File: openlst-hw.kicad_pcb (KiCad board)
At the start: 4 copper layers, 85 x 85 mm, 123 parts, among them J1 Conn_02x20_Odd_Even, J10 EXT VBUS, J2 EXT 3.3V, J3 UART0, J4 UART1, J5 Switch Select, J6 Control Outputs, J7 CC Prog/Debug, J8 Conn_Coaxial, J9 ANT, U1 ADP150AUJZ-3.3-R7, U2 CC1110, U3 0433BM15A0001, U4 MIC803, U5 PE4250MLI, U6 PE4250MLI, U7 SF2446E, U8 RFFM6406, X1 TG2520SMN 27MHz

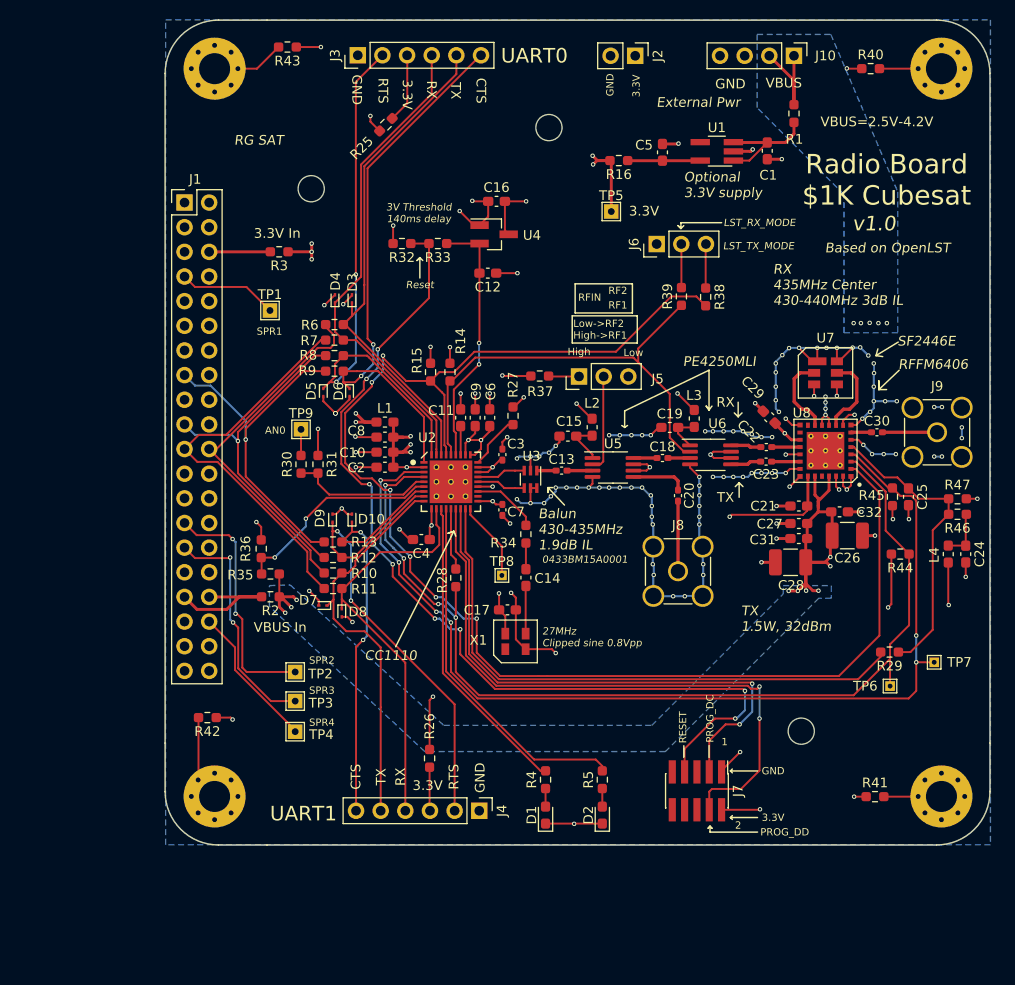
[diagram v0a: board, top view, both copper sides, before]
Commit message: upgrade to KICAD 8, change power converters and auxiliarry pin connectors
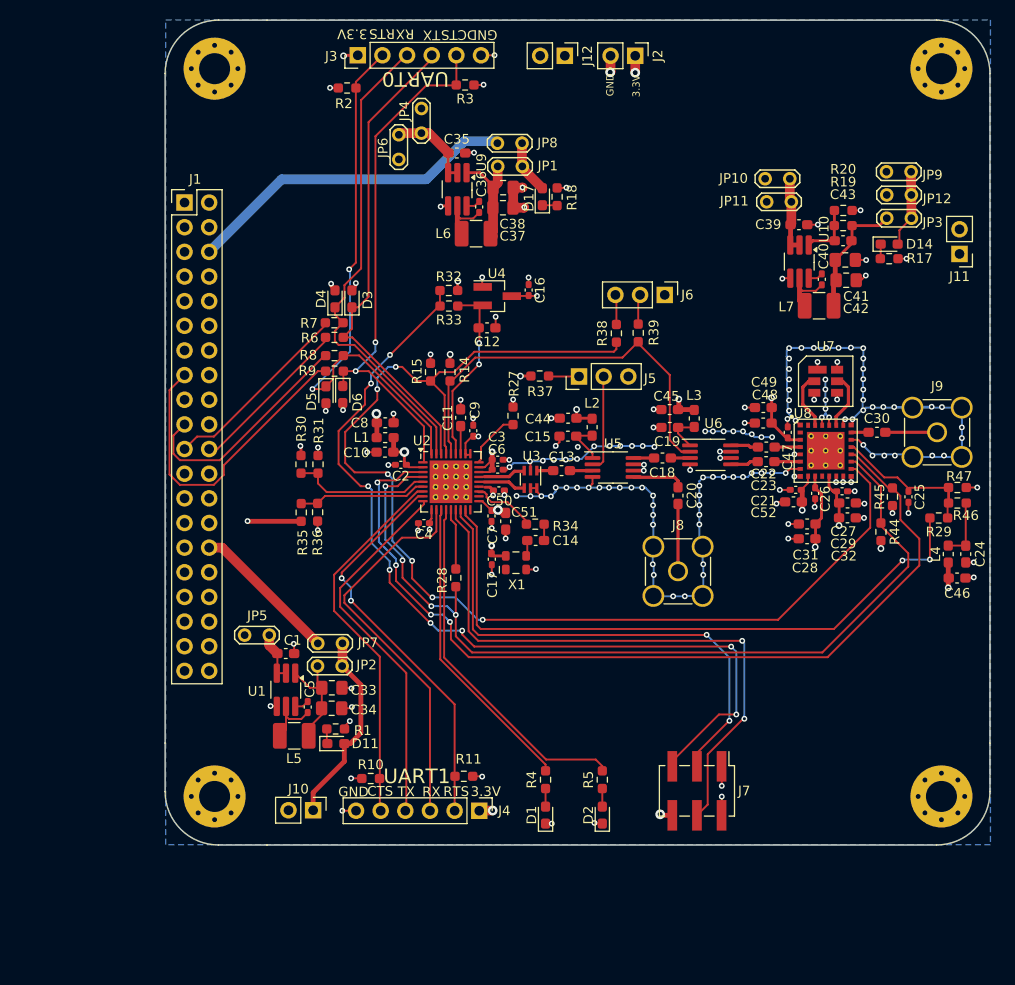
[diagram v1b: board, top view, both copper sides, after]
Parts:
- removed D10, D7, D8, D9: ESD9B5.0ST5G, Diode_SMD:D_SOD-923
- removed H5, H6, H7: MountingHole, MountingHole:MountingHole_2.7mm
- removed LOGO1: Logo_Open_Hardware_Small, footprint_custom:a1
- removed LOGO2: Logo_Open_Hardware_Small, footprint_custom:a2
- removed LOGO3: Logo_Open_Hardware_Small, Symbol:OSHW-Logo2_24.3x20mm_SilkScreen
- removed R12, R13, R25, R26, R40, R41, R42, R43: DNP, Resistor_SMD:R_0603_1608Metric_Pad0.98x0.95mm_HandSolder
- removed R16: 0, Resistor_SMD:R_0603_1608Metric_Pad0.98x0.95mm_HandSolder
- removed TP1, TP2, TP3, TP4, TP5, TP9: TP_1.5x1.5, TestPoint:TestPoint_THTPad_1.5x1.5mm_Drill0.7mm
- removed TP6, TP7, TP8: TP_tht_1x1, TestPoint:TestPoint_THTPad_1.0x1.0mm_Drill0.5mm
- added C33: 22u, Capacitor_SMD:C_0805_2012Metric_Pad1.18x1.45mm_HandSolder, F.Cu at (88.1, 114.8)
- added C34: 22u, Capacitor_SMD:C_0805_2012Metric_Pad1.18x1.45mm_HandSolder, F.Cu at (88.1, 116.9)
- added C35: 10u, Capacitor_SMD:C_0603_1608Metric_Pad1.08x0.95mm_HandSolder, F.Cu at (101.0, 59.7)
- added C36: 100n, Capacitor_SMD:C_0402_1005Metric_Pad0.74x0.62mm_HandSolder, F.Cu at (103.3, 65.3)
- added C37: 22u, Capacitor_SMD:C_0805_2012Metric_Pad1.18x1.45mm_HandSolder, F.Cu at (105.8, 65.4)
- added C38: 22u, Capacitor_SMD:C_0805_2012Metric_Pad1.18x1.45mm_HandSolder, F.Cu at (105.8, 63.3)
- added C39: 10u, Capacitor_SMD:C_0603_1608Metric_Pad1.08x0.95mm_HandSolder, F.Cu at (136.3, 67.1)
- added C40: 100n, Capacitor_SMD:C_0402_1005Metric_Pad0.74x0.62mm_HandSolder, F.Cu at (138.6, 72.7)
- added C41: 22u, Capacitor_SMD:C_0805_2012Metric_Pad1.18x1.45mm_HandSolder, F.Cu at (141.0, 70.7)
- added C42: 22u, Capacitor_SMD:C_0805_2012Metric_Pad1.18x1.45mm_HandSolder, F.Cu at (141.1, 72.8)
- added C43: 100p, Capacitor_SMD:C_0603_1608Metric_Pad1.08x0.95mm_HandSolder, F.Cu at (140.8, 68.8)
- added C44: 1u, Capacitor_SMD:C_0603_1608Metric_Pad1.08x0.95mm_HandSolder, F.Cu at (112.5, 87.0)
- added C45: 1u, Capacitor_SMD:C_0603_1608Metric_Pad1.08x0.95mm_HandSolder, F.Cu at (122.9, 86.2)
- added C46: 1u, Capacitor_SMD:C_0603_1608Metric_Pad1.08x0.95mm_HandSolder, F.Cu at (152.6, 103.5)
- added C47: 100n, Capacitor_SMD:C_0402_1005Metric_Pad0.74x0.62mm_HandSolder, F.Cu at (135.1, 88.5)
- added C48: 10u, Capacitor_SMD:C_0603_1608Metric_Pad1.08x0.95mm_HandSolder, F.Cu at (132.6, 87.5)
- added C49: 47u, Capacitor_SMD:C_0603_1608Metric_Pad1.08x0.95mm_HandSolder, F.Cu at (132.6, 86.0)
- added C50: 100n, Capacitor_SMD:C_0402_1005Metric_Pad0.74x0.62mm_HandSolder, F.Cu at (105.3, 94.5)
- added C51: 10u, Capacitor_SMD:C_0603_1608Metric_Pad1.08x0.95mm_HandSolder, F.Cu at (106.0, 97.7)
- added C52: 10u, Capacitor_SMD:C_0603_1608Metric_Pad1.08x0.95mm_HandSolder, F.Cu at (135.7, 95.7)
- added D11: GREEN V4, LED_SMD:LED_0603_1608Metric_Pad1.05x0.95mm_HandSolder, F.Cu at (88.5, 120.6)
- added D14: GREEN V4, LED_SMD:LED_0603_1608Metric_Pad1.05x0.95mm_HandSolder, F.Cu at (145.6, 69.1)
- added D17: GREEN V3, LED_SMD:LED_0603_1608Metric_Pad1.05x0.95mm_HandSolder, F.Cu at (109.8, 64.2)
- added J11: EXT VRF, Connector_PinHeader_2.54mm:PinHeader_1x02_P2.54mm_Vertical, F.Cu at (152.8, 70.1)
- added J12: EXT VBAT, Connector_PinHeader_2.54mm:PinHeader_1x02_P2.54mm_Vertical, F.Cu at (112.1, 49.7)
- added JP1: Jumper_2_Open, TestPoint:TestPoint_2Pads_Pitch2.54mm_Drill0.8mm, F.Cu at (105.2, 61.1)
- added JP10: Jumper_2_Open, TestPoint:TestPoint_2Pads_Pitch2.54mm_Drill0.8mm, F.Cu at (132.8, 62.4)
- added JP11: Jumper_2_Open, TestPoint:TestPoint_2Pads_Pitch2.54mm_Drill0.8mm, F.Cu at (132.9, 64.8)
- added JP12: Jumper_2_Open, TestPoint:TestPoint_2Pads_Pitch2.54mm_Drill0.8mm, F.Cu at (145.3, 64.0)
- added JP2: Jumper_2_Open, TestPoint:TestPoint_2Pads_Pitch2.54mm_Drill0.8mm, F.Cu at (86.7, 112.6)
- added JP3: Jumper_2_Open, TestPoint:TestPoint_2Pads_Pitch2.54mm_Drill0.8mm, F.Cu at (145.3, 66.4)
- added JP4: Jumper_2_Open, TestPoint:TestPoint_2Pads_Pitch2.54mm_Drill0.8mm, F.Cu at (97.4, 55.1)
- added JP5: Jumper_2_Open, TestPoint:TestPoint_2Pads_Pitch2.54mm_Drill0.8mm, F.Cu at (79.1, 109.4)
- added JP6: Jumper_2_Open, TestPoint:TestPoint_2Pads_Pitch2.54mm_Drill0.8mm, F.Cu at (95.0, 60.4)
- added JP7: Jumper_2_Open, TestPoint:TestPoint_2Pads_Pitch2.54mm_Drill0.8mm, F.Cu at (86.7, 110.2)
- added JP8: Jumper_2_Open, TestPoint:TestPoint_2Pads_Pitch2.54mm_Drill0.8mm, F.Cu at (105.2, 58.7)
- added JP9: Jumper_2_Open, TestPoint:TestPoint_2Pads_Pitch2.54mm_Drill0.8mm, F.Cu at (145.3, 61.6)
- added L5: 4.7uH, Inductor_SMD:L_1210_3225Metric_Pad1.42x2.65mm_HandSolder, F.Cu at (84.3, 119.8)
- added L6: 3.9uH, Inductor_SMD:L_1210_3225Metric_Pad1.42x2.65mm_HandSolder, F.Cu at (103.0, 68.0)
- added L7: 4.7uH, Inductor_SMD:L_1210_3225Metric_Pad1.42x2.65mm_HandSolder, F.Cu at (138.3, 75.5)
- added R17: 1K2, Resistor_SMD:R_0603_1608Metric_Pad0.98x0.95mm_HandSolder, F.Cu at (145.6, 70.6)
- added R18: 680, Resistor_SMD:R_0603_1608Metric_Pad0.98x0.95mm_HandSolder, F.Cu at (111.3, 64.2)
- added R19: 165K, Resistor_SMD:R_0603_1608Metric_Pad0.98x0.95mm_HandSolder, F.Cu at (140.8, 67.2)
- added R20: 33K, Resistor_SMD:R_0603_1608Metric_Pad0.98x0.95mm_HandSolder, F.Cu at (140.8, 65.6)
- added U10: AP63200WU, Package_TO_SOT_SMD:TSOT-23-6_HandSoldering, F.Cu at (136.3, 70.9)
- added U9: AP63203WU, Package_TO_SOT_SMD:TSOT-23-6_HandSoldering, F.Cu at (101.1, 63.5)
- C1: value 4.7uF -> 10u
- C10, C11, C8: value 1uF -> 1u
- C12, C14: value 0.01uF -> 10n
- C13, C18, C20, C22, C23, C30: value 220pF -> 220p; footprint Capacitor_SMD:C_0402_1005Metric_Pad0.74x0.62mm_HandSolder -> Capacitor_SMD:C_0603_1608Metric_Pad1.08x0.95mm_HandSolder
- C15, C19, C24: value 0.1uF -> 1u
- C16, C17, C2, C21, C25, C4, C6, C9: value 0.1uF -> 100n; footprint Capacitor_SMD:C_0603_1608Metric_Pad1.08x0.95mm_HandSolder -> Capacitor_SMD:C_0402_1005Metric_Pad0.74x0.62mm_HandSolder
- C26: value 47uF -> 100n; footprint Capacitor_SMD:C_1210_3225Metric_Pad1.33x2.70mm_HandSolder -> Capacitor_SMD:C_0402_1005Metric_Pad0.74x0.62mm_HandSolder
- C27: value 1uF -> 100n; footprint Capacitor_SMD:C_0603_1608Metric_Pad1.08x0.95mm_HandSolder -> Capacitor_SMD:C_0402_1005Metric_Pad0.74x0.62mm_HandSolder
- C28: value 47uF -> 10u; footprint Capacitor_SMD:C_1210_3225Metric_Pad1.33x2.70mm_HandSolder -> Capacitor_SMD:C_0603_1608Metric_Pad1.08x0.95mm_HandSolder
- C29: value 0.1uF -> 10u
- C3, C7: value 220pF -> 100n
- C31: value 4.7uF -> 47u
- C32: value 0.1uF -> 47u
- C5: value 4.7uF -> 100n; footprint Capacitor_SMD:C_0603_1608Metric_Pad1.08x0.95mm_HandSolder -> Capacitor_SMD:C_0402_1005Metric_Pad0.74x0.62mm_HandSolder
- D1, D2: value LED_SMD_RED -> ORANGE
- D3, D4, D5, D6: footprint Diode_SMD:D_SOD-923 -> LED_SMD:LED_0603_1608Metric_Pad1.05x0.95mm_HandSolder
- J10: value EXT VBUS -> EXT 5V; footprint Connector_PinHeader_2.54mm:PinHeader_1x04_P2.54mm_Vertical -> Connector_PinHeader_2.54mm:PinHeader_1x02_P2.54mm_Vertical
- J2: value EXT 3.3V -> EXT 3V3
- J7: footprint Connector_PinHeader_1.27mm:PinHeader_2x05_P1.27mm_Vertical_SMD -> Connector_PinHeader_2.54mm:PinHeader_2x03_P2.54mm_Vertical_SMD
- R1: value DNP -> 1k5
- R10, R11: value DNP -> 20K
- R2, R3: value 10m -> 20K
- R30: value DNP -> 13K7
- R31: value DNP -> 26K7
- R35: value 20K -> 137K
- R36: value 47K -> 20K
- R37: value 1K -> 20K
- R38, R39, R6, R7, R8, R9: value 100 -> 22
- R4, R5: value 1K -> 680
- U1: value ADP150AUJZ-3.3-R7 -> AP63205WU; footprint Package_TO_SOT_SMD:TSOT-23-5_HandSoldering -> Package_TO_SOT_SMD:TSOT-23-6_HandSoldering
- U2: footprint openlst:TI_CC_QFN36 -> Project:Texas_RHH0036C_VQFN-36-1EP_6x6mm_P0.5mm_EP4.4x4.4mm_ThermalVias
- U7: footprint footprint_custom:SF2446E -> Project:SF2446E
- U8: footprint openlst:Qorvo_LGA_28_ThermalVias -> Project:RFFM6406
- X1: footprint footprint_custom:TG2520SMN -> Project:Oscillator_SMD_SeikoEpson_TG2520SMN-xxx-xxxxxx-4Pin_2.5x2.0mm
- moved J10 92.2 mm to (86.2, 127.5)
- moved R1 79.1 mm to (88.5, 119.1), turned to 0 degrees
- moved C1 71.7 mm to (83.4, 111.3), turned to 0 degrees
- moved U1 71.1 mm to (83.4, 115.0), turned to -90 degrees
- moved C5 67.9 mm to (85.6, 116.8)
- moved R2 53.0 mm to (89.7, 53.0), turned to 0 degrees
- moved R3 25.7 mm to (101.9, 52.7)
- moved R11 23.6 mm to (101.7, 124.0), turned to 180 degrees
- moved R10 21.5 mm to (92.1, 124.2)
- moved R29 14.7 mm to (150.7, 97.3)
- moved C29 12.0 mm to (141.3, 95.8), turned to 0 degrees
- moved R38 9.93 mm to (117.5, 78.3)
- moved C16 9.72 mm to (108.4, 73.8), turned to -90 degrees
- moved X1 8.11 mm to (107.1, 101.9), turned to 90 degrees
- moved R35 7.09 mm to (85.0, 96.8), turned to -90 degrees
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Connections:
- net /~LST_RX_MODE renamed /~{LST_RX_MODE}
- C1 pad 1: Net-(C1-Pad1) -> +VBAT
- C10 pad 1: /3V3_FILT -> /+3V3_C1110
- C2 pad 1: /3V3_FILT -> /+3V3_C1110
- C26 pad 1: VBUS -> VRF
- C27 pad 1: VBUS -> VRF
- C28 pad 1: VBUS -> VRF
- C29 pad 1: VBUS -> VRF
- C3 pad 1: /3V3_FILT -> /+3V3_C1110
- C31 pad 1: VBUS -> VRF
- C32 pad 1: VBUS -> VRF
- C4 pad 1: /3V3_FILT -> /+3V3_C1110
- C5 pad 2: GND -> Net-(U1-BST)
- C6 pad 1: /3V3_FILT -> /+3V3_C1110
- C7 pad 1: /3V3_FILT -> /+3V3_C1110
- C8 pad 1: /3V3_FILT -> +3V3
- C9 pad 1: /3V3_FILT -> /+3V3_C1110
- D3 pad 1: /UART0_TX -> UART0_TX
- D4 pad 1: /UART0_RX -> UART0_RX
- D5 pad 1: /UART0_RTS -> UART0_RTS
- D6 pad 1: /UART0_CTS -> UART0_CTS
- H1 pad 1: Net-(H1-Pad1) -> GND
- H2 pad 1: Net-(H2-Pad1) -> GND
- H3 pad 1: Net-(H3-Pad1) -> GND
- H4 pad 1: Net-(H4-Pad1) -> GND
- J1 pad 1: (no net) -> /INTERBOARD_CONNECTOR2/3V3_11
- J1 pad 11: (no net) -> /INTERBOARD_CONNECTOR2/3V3_3
- J1 pad 12: (no net) -> /INTERBOARD_CONNECTOR2/EPS_RESET
- J1 pad 13: (no net) -> /INTERBOARD_CONNECTOR2/UART_A_TXO
- J1 pad 14: (no net) -> /INTERBOARD_CONNECTOR2/UART_A_RXI
- J1 pad 16: (no net) -> /INTERBOARD_CONNECTOR2/AVI_RESET
- J1 pad 18: (no net) -> /INTERBOARD_CONNECTOR2/3V3_12
- J1 pad 2: (no net) -> /INTERBOARD_CONNECTOR2/3V3_5
- J1 pad 23: (no net) -> /INTERBOARD_CONNECTOR2/3V3_6
- J1 pad 24: (no net) -> /INTERBOARD_CONNECTOR2/3V3_2
- J1 pad 25: (no net) -> /INTERBOARD_CONNECTOR2/3V3_8
- J1 pad 26: (no net) -> /INTERBOARD_CONNECTOR2/3V3_1
- J1 pad 30: (no net) -> 5V0
- J1 pad 33: /INTERBOARD_CONNECTOR2/5V0_2 -> VBAT
- J1 pad 34: /INTERBOARD_CONNECTOR2/5V0_2 -> VBAT
- J1 pad 39: (no net) -> /INTERBOARD_CONNECTOR2/CANL
- J1 pad 40: (no net) -> /INTERBOARD_CONNECTOR2/CANH
- J1 pad 5: (no net) -> /INTERBOARD_CONNECTOR2/3V3_4
- J1 pad 6: /INTERBOARD_CONNECTOR2/3V3_10 -> 3V3
- J1 pad 8: (no net) -> /INTERBOARD_CONNECTOR2/3V3_7
- J1 pad 9: (no net) -> /INTERBOARD_CONNECTOR2/3V3_9
- J10 pad 1: VBUS -> +5V
- J10 pad 2: VBUS -> GND
- J3 pad 1: GND -> +3V3
- J3 pad 2: /UART0_RTS -> UART0_RTS
- J3 pad 3: Net-(J3-Pad3) -> UART0_RX
- J3 pad 4: /UART0_RX -> UART0_TX
- J3 pad 5: /UART0_TX -> UART0_CTS
- J3 pad 6: /UART0_CTS -> GND
- J4 pad 1: GND -> +3V3
- J4 pad 2: /UART1_RTS -> UART1_RTS
- J4 pad 3: Net-(J4-Pad3) -> UART1_RX
- J4 pad 4: /UART1_RX -> UART1_TX
- J4 pad 5: /UART1_TX -> UART1_CTS
- J4 pad 6: /UART1_CTS -> GND
- J7 pad 2: +3V3 -> GND
- J7 pad 5: (no net) -> /~{LST_RESET}
- J7 pad 6: (no net) -> +3V3
- L1 pad 2: /3V3_FILT -> /+3V3_C1110
- R1 pad 1: Net-(C1-Pad1) -> Net-(D11-K)
- R1 pad 2: VBUS -> GND
- R10 pad 1: /INTERBOARD_CONNECTOR2/UART_B_RXI -> GND
- R10 pad 2: /UART1_TX -> UART1_CTS
- R11 pad 1: /INTERBOARD_CONNECTOR2/UART_B_TXO -> GND
- R11 pad 2: /UART1_RX -> UART1_RTS
- R2 pad 1: VBUS -> GND
- R2 pad 2: /INTERBOARD_CONNECTOR2/5V0_2 -> UART0_RTS
- R27 pad 1: Net-(R27-Pad1) -> GND
- R27 pad 2: GND -> Net-(U2-RBIAS)
- R3 pad 1: +3V3 -> GND
- R3 pad 2: /INTERBOARD_CONNECTOR2/3V3_10 -> UART0_CTS
- R30 pad 2: Net-(R30-Pad2) -> VRF
- R32 pad 1: /~LST_RESET -> /~{LST_RESET}
- R33 pad 2: /~LST_RESET -> /~{LST_RESET}
- R35 pad 2: VBUS -> +VBAT
- R6 pad 1: /UART0_TX -> UART0_TX
- R7 pad 1: /UART0_RX -> UART0_RX
- R8 pad 1: /UART0_RTS -> UART0_RTS
- R9 pad 1: /UART0_CTS -> UART0_CTS
- U1 pad 1: Net-(C1-Pad1) -> Net-(JP2-A)
- U1 pad 2: GND -> +VBAT
- U1 pad 3: Net-(C1-Pad1) -> +VBAT
- U1 pad 4: (no net) -> GND
- U2 pad 1: /UART0_CTS -> UART0_CTS
- U2 pad 10: /3V3_FILT -> /+3V3_C1110
- U2 pad 11: /UART1_RX -> UART1_RX
- U2 pad 18: Net-(TP8-Pad1) -> unconnected-(U2-P2_4/XOSC32-2-Pad18)
- U2 pad 19: /3V3_FILT -> /+3V3_C1110
- U2 pad 2: /3V3_FILT -> /+3V3_C1110
- U2 pad 20: (no net) -> unconnected-(U2-XOSC-2-Pad20)
- U2 pad 22: /3V3_FILT -> /+3V3_C1110
- U2 pad 25: /3V3_FILT -> /+3V3_C1110
- U2 pad 26: /3V3_FILT -> /+3V3_C1110
- U2 pad 27: Net-(R27-Pad1) -> Net-(U2-RBIAS)
- U2 pad 28: /3V3_FILT -> /+3V3_C1110
- U2 pad 29: /3V3_FILT -> /+3V3_C1110
- U2 pad 34: /UART0_TX -> UART0_TX
- U2 pad 35: /UART0_RX -> UART0_RX
- U2 pad 36: /UART0_RTS -> UART0_RTS
- U2 pad 7: /UART1_CTS -> UART1_CTS
- U2 pad 8: /UART1_RTS -> UART1_RTS
- U2 pad 9: /UART1_TX -> UART1_TX
- U8 pad 14: (no net) -> unconnected-(U8-NC-Pad14)
- U8 pad 16: (no net) -> unconnected-(U8-NC-Pad16)
- U8 pad 17: VBUS -> VRF
- U8 pad 24: VBUS -> VRF
- U8 pad 25: (no net) -> unconnected-(U8-NC-Pad25)
- U8 pad 26: VBUS -> VRF
- X1 pad 1: (no net) -> unconnected-(X1-NC-Pad1)
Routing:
- net +VBAT: track 0.00 -> 141.6 mm, vias 0 -> 1
- net +5V: track 0.00 -> 137.0 mm
- net /~LST_RESET: track 97.5 -> 0.00 mm, vias 8 -> 0
- net VRF: track 0.00 -> 94.9 mm, vias 0 -> 4
- net /~{LST_RESET}: track 0.00 -> 91.5 mm, vias 0 -> 8
- net VBUS: track 58.2 -> 0.00 mm, vias 15 -> 0
- net UART0_RTS: track 0.00 -> 57.8 mm, vias 0 -> 2
- net /UART0_CTS: track 57.8 -> 0.00 mm, vias 2 -> 0
- net /UART0_RTS: track 56.0 -> 0.00 mm, vias 2 -> 0
- net UART0_CTS: track 0.00 -> 54.6 mm, vias 0 -> 2
- net /UART0_TX: track 51.6 -> 0.00 mm
- net /UART0_RX: track 50.4 -> 0.00 mm
- net UART0_RX: track 0.00 -> 50.3 mm
- net UART0_TX: track 0.00 -> 50.0 mm
- net /UART1_RTS: track 49.4 -> 0.00 mm, vias 2 -> 0
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- added copper zone on In2.Cu, net /+3V3_C1110
- added copper zone on In2.Cu, net VRF
- removed copper zone on In2.Cu, net /3V3_FILT
- removed copper zone on B.Cu, net VBUS
- removed copper zone on In2.Cu, net VBUS
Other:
- net class 50ohm removed
- net class 8mil removed
- net class Default removed
- net class PWR removed
- rule pad_to_mask_clearance: 0.0508 -> 0
- board text removed: "0433BM15A0001"
- board text removed: "1"
- board text removed: "2"
- board text removed: "27MHz Clipped sine 0.8Vpp"
- board text removed: "3.3V In"
- board text removed: "3V Threshold 140ms delay"
- board text removed: "AN0"
- board text removed: "Always has been"
- board text removed: "Balun 430-435MHz 1.9dB IL"
- board text removed: "Based on OpenLST"
- board text removed: "CC1110"
- board text removed: "External Pwr"
- board text removed: "High"
- board text removed: "LST_RX_MODE"
- board text removed: "LST_TX_MODE"
- board text removed: "Low"
- board text removed: "Low->RF2 High->RF1"
- board text removed: "Optional 3.3V supply"
- board text removed: "PE4250MLI"
- board text removed: "PROG_DC"
- board text removed: "PROG_DD"
- board text removed: "RESET"
- board text removed: "RF1"
- board text removed: "RF2"
- board text removed: "RFFM6406"
- board text removed: "RFIN"
- board text removed: "RG SAT"
- board text removed: "RX 435MHz Center 430-440MHz 3dB IL"
- board text removed: "Radio Board $1K Cubesat"
- board text removed: "Reset"
- board text removed: "SF2446E"
- board text removed: "SPR1"
- board text removed: "SPR2"
- board text removed: "SPR3"
- board text removed: "SPR4"
- board text removed: "TX 1.5W, 32dBm"
- board text removed: "VBUS"
- board text removed: "VBUS In"
- board text removed: "VBUS=2.5V-4.2V"
- board text removed: "Wait, it's all open source?"
- board text removed: "subscribe"
- board text removed: "v1.0"

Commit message: change footprint to 80x80mm to fit cubesat 1U more comfortabley
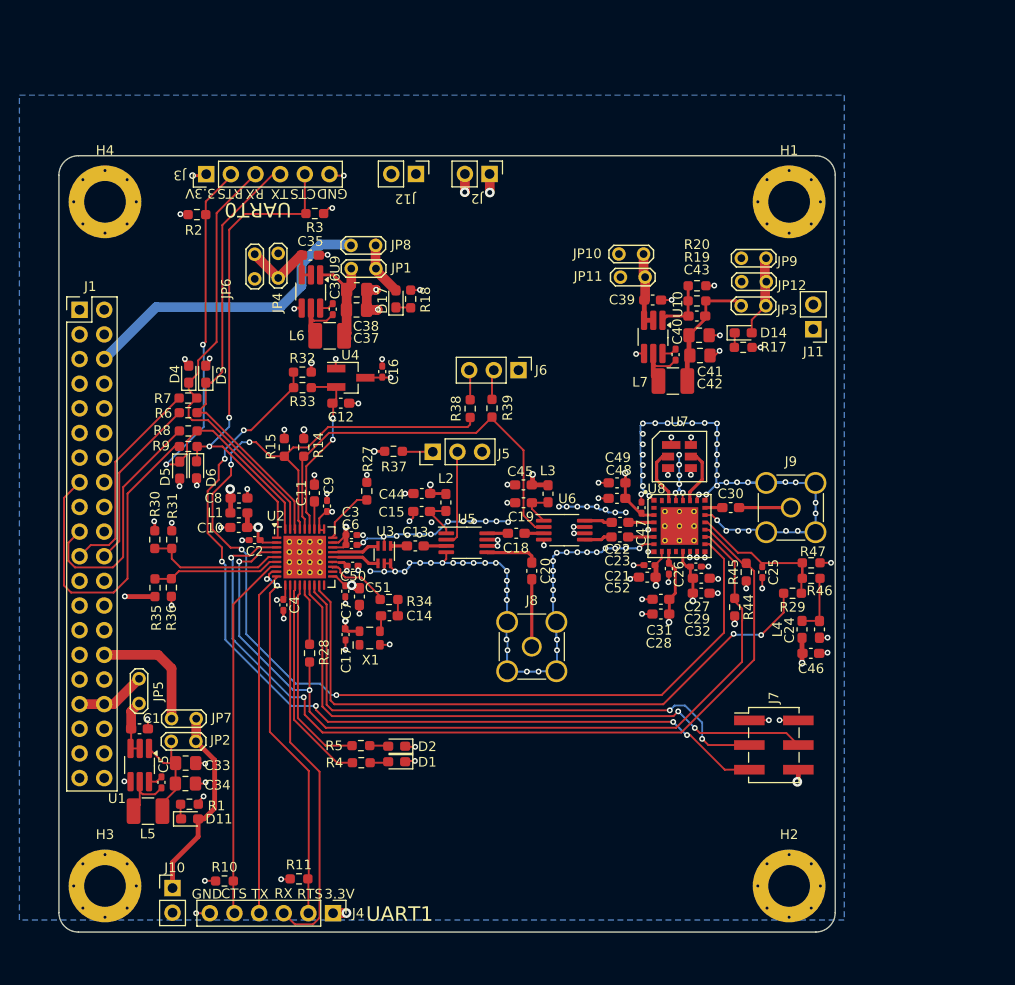
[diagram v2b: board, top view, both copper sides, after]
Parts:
- H1, H2, H3, H4: footprint MountingHole:MountingHole_3.2mm_M3_Pad_Via -> Project:MountingHole_4.3mm_M4_Pad_Via_Custom
- moved R5 25.1 mm to (91.1, 120.8), turned to 180 degrees
- moved D2 22.3 mm to (94.8, 120.8), turned to 180 degrees
- moved JP4 21.0 mm to (82.6, 70.1)
- moved H1 20.8 mm to (135.2, 64.8)
- moved R3 20.4 mm to (86.4, 66.0)
- moved R2 20.2 mm to (74.2, 66.1)
- moved R11 20.0 mm to (84.7, 134.5), turned to 0 degrees
- moved J3 19.9 mm to (75.2, 61.9)
- moved J12 19.6 mm to (96.8, 61.9)
- moved J2 19.3 mm to (104.4, 61.9)
- moved JP6 19.3 mm to (80.2, 72.7)
- moved R4 19.1 mm to (91.2, 122.5), turned to 180 degrees
- moved J4 18.4 mm to (88.2, 138.1)
- moved R10 18.4 mm to (77.1, 134.7)
- moved C35 18.4 mm to (85.9, 70.2)
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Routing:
- net Net-(U2-P0_7): track 36.8 -> 20.6 mm
- net +5V: track 137.0 -> 122.3 mm
- net +VBAT: track 141.6 -> 128.5 mm
- net Net-(U2-P0_6): track 31.5 -> 21.9 mm
- net /PROG_DC: track 52.5 -> 60.3 mm
- net UART0_RX: track 50.3 -> 45.6 mm
- net UART0_RTS: track 57.8 -> 53.4 mm
- net UART0_TX: track 50.0 -> 45.7 mm
- net GND: track 233.0 -> 229.9 mm
- net UART1_TX: track 38.3 -> 35.5 mm
- net UART0_CTS: track 54.6 -> 51.8 mm
- net 3V3: track 34.4 -> 31.7 mm
- net 5V0: track 15.3 -> 12.7 mm
- net UART1_RTS: track 41.1 -> 38.7 mm
- net /PROG_DD: track 61.9 -> 64.3 mm
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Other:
- board size 85 x 85 mm -> 80 x 80 mm

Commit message: add CAN bridge, change bus connector from 2x20 to 2x24 to allow second can bus and battery
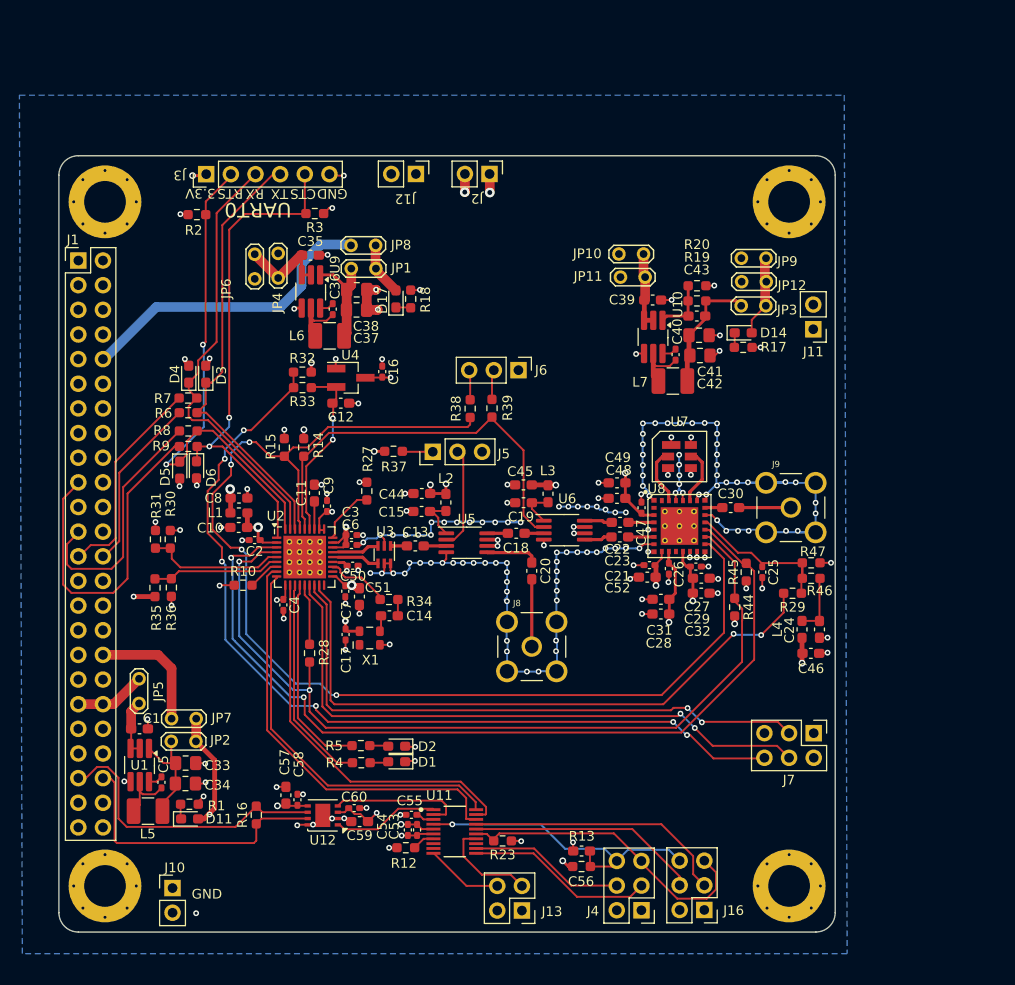
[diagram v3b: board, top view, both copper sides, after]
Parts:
- removed R11: 20K, Resistor_SMD:R_0603_1608Metric_Pad0.98x0.95mm_HandSolder
- added C53: 100n, Capacitor_SMD:C_0402_1005Metric_Pad0.74x0.62mm_HandSolder, F.Cu at (96.9, 129.5)
- added C54: 10u, Capacitor_SMD:C_0402_1005Metric_Pad0.74x0.62mm_HandSolder, F.Cu at (96.0, 129.5)
- added C55: 470n, Capacitor_SMD:C_0402_1005Metric_Pad0.74x0.62mm_HandSolder, F.Cu at (96.3, 127.9)
- added C56: 10n, Capacitor_SMD:C_0603_1608Metric_Pad1.08x0.95mm_HandSolder, F.Cu at (113.9, 131.7)
- added C57: 10u, Capacitor_SMD:C_0603_1608Metric_Pad1.08x0.95mm_HandSolder, F.Cu at (83.4, 125.9)
- added C58: 100n, Capacitor_SMD:C_0402_1005Metric_Pad0.74x0.62mm_HandSolder, F.Cu at (84.6, 126.4)
- added C59: 10u, Capacitor_SMD:C_0603_1608Metric_Pad1.08x0.95mm_HandSolder, F.Cu at (91.0, 128.6)
- added C60: 100n, Capacitor_SMD:C_0402_1005Metric_Pad0.74x0.62mm_HandSolder, F.Cu at (90.4, 127.2)
- added J13: MS UART1, Connector_PinHeader_2.54mm:PinHeader_2x02_P2.54mm_Vertical, F.Cu at (107.7, 137.8)
- added J16: MS Prog/Debug, Connector_PinHeader_2.54mm:PinHeader_2x03_P2.54mm_Vertical, F.Cu at (126.5, 137.7)
- added R12: 100k, Resistor_SMD:R_0603_1608Metric_Pad0.98x0.95mm_HandSolder, F.Cu at (95.8, 131.3)
- added R13: 47k, Resistor_SMD:R_0603_1608Metric_Pad0.98x0.95mm_HandSolder, F.Cu at (113.9, 133.2)
- added R16: 120, Resistor_SMD:R_0603_1608Metric_Pad0.98x0.95mm_HandSolder, F.Cu at (80.3, 127.9)
- added R23: 47k, Resistor_SMD:R_0603_1608Metric_Pad0.98x0.95mm_HandSolder, F.Cu at (105.7, 130.6)
- added U11: MSPM0G3107SDGS20R, Project:DGS0020A-MFG, F.Cu at (100.8, 129.6)
- added U12: TJA1051TK-3, Package_DFN_QFN:DFN-8-1EP_3x3mm_P0.65mm_EP1.55x2.4mm, F.Cu at (87.2, 128.0)
- J1: value Conn_02x20_Odd_Even -> Conn_02x24_Odd_Even; footprint Connector_PinHeader_2.54mm:PinHeader_2x20_P2.54mm_Vertical -> Connector_PinHeader_2.54mm:PinHeader_2x24_P2.54mm_Vertical
- J4: value UART1 -> MS UART0; footprint Connector_PinHeader_2.54mm:PinHeader_1x06_P2.54mm_Vertical -> Connector_PinHeader_2.54mm:PinHeader_2x03_P2.54mm_Vertical
- J7: footprint Connector_PinHeader_2.54mm:PinHeader_2x03_P2.54mm_Vertical_SMD -> Connector_PinHeader_2.54mm:PinHeader_2x03_P2.54mm_Vertical
- J8, J9: footprint Connector_Coaxial:SMA_Amphenol_901-144_Vertical -> Project:LINX_CONSMA001-G
- moved J4 31.8 mm to (120.0, 137.8), turned to 180 degrees
- moved R10 30.5 mm to (79.0, 104.3)
- moved J1 5.08 mm to (62.0, 70.8)
- moved J7 4.29 mm to (137.8, 119.5), turned to -90 degrees
- moved R31 1.68 mm to (70.0, 99.5)
- moved R30 1.60 mm to (71.5, 99.5)
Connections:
- net UART0_CTS renamed /UART0_CTS
- net UART0_RTS renamed /UART0_RTS
- net UART0_RX renamed /UART0_RX
- net UART0_TX renamed /UART0_TX
- J1 pad 1: /INTERBOARD_CONNECTOR2/3V3_11 -> unconnected-(J1-Pin_1-Pad1)
- J1 pad 10: GND -> 3V3
- J1 pad 11: /INTERBOARD_CONNECTOR2/3V3_3 -> /INTERBOARD_CONNECTOR2/SPARE_1
- J1 pad 12: /INTERBOARD_CONNECTOR2/EPS_RESET -> /INTERBOARD_CONNECTOR2/3V3_7
- J1 pad 13: /INTERBOARD_CONNECTOR2/UART_A_TXO -> /INTERBOARD_CONNECTOR2/3V3_9
- J1 pad 14: /INTERBOARD_CONNECTOR2/UART_A_RXI -> GND
- J1 pad 15: /INTERBOARD_CONNECTOR2/UART_B_RTS -> /INTERBOARD_CONNECTOR2/3V3_3
- J1 pad 16: /INTERBOARD_CONNECTOR2/AVI_RESET -> /INTERBOARD_CONNECTOR2/EPS_RESET
- J1 pad 17: GND -> /INTERBOARD_CONNECTOR2/UART_A_TXO
- J1 pad 18: /INTERBOARD_CONNECTOR2/3V3_12 -> /INTERBOARD_CONNECTOR2/UART_A_RXI
- J1 pad 19: /INTERBOARD_CONNECTOR2/UART_B_CTS -> /INTERBOARD_CONNECTOR2/UART_B_RTS
- J1 pad 2: /INTERBOARD_CONNECTOR2/3V3_5 -> unconnected-(J1-Pin_2-Pad2)
- J1 pad 20: GND -> /INTERBOARD_CONNECTOR2/AVI_RESET
- J1 pad 21: /INTERBOARD_CONNECTOR2/UART_B_TXO -> GND
- J1 pad 22: /INTERBOARD_CONNECTOR2/UART_B_RXI -> /INTERBOARD_CONNECTOR2/3V3_12
- J1 pad 23: /INTERBOARD_CONNECTOR2/3V3_6 -> /INTERBOARD_CONNECTOR2/UART_B_CTS
- J1 pad 24: /INTERBOARD_CONNECTOR2/3V3_2 -> GND
- J1 pad 25: /INTERBOARD_CONNECTOR2/3V3_8 -> /INTERBOARD_CONNECTOR2/UART_B_TXO
- J1 pad 26: /INTERBOARD_CONNECTOR2/3V3_1 -> /INTERBOARD_CONNECTOR2/UART_B_RXI
- J1 pad 27: /INTERBOARD_CONNECTOR2/SPARE_2 -> /INTERBOARD_CONNECTOR2/3V3_6
- J1 pad 28: GND -> /INTERBOARD_CONNECTOR2/3V3_2
- J1 pad 29: /INTERBOARD_CONNECTOR2/SPARE_3 -> /INTERBOARD_CONNECTOR2/3V3_8
- J1 pad 3: GND -> unconnected-(J1-Pin_3-Pad3)
- J1 pad 30: 5V0 -> /INTERBOARD_CONNECTOR2/3V3_1
- J1 pad 31: GND -> /INTERBOARD_CONNECTOR2/SPARE_2
- J1 pad 33: VBAT -> /INTERBOARD_CONNECTOR2/SPARE_3
- J1 pad 34: VBAT -> 5V0
- J1 pad 36: /INTERBOARD_CONNECTOR2/SPARE_4 -> GND
- J1 pad 37: GND -> VBAT
- J1 pad 38: GND -> VBAT
- J1 pad 39: /INTERBOARD_CONNECTOR2/CANL -> GND
- J1 pad 4: GND -> unconnected-(J1-Pin_4-Pad4)
- J1 pad 40: /INTERBOARD_CONNECTOR2/CANH -> /INTERBOARD_CONNECTOR2/SPARE_4
- J1 pad 5: /INTERBOARD_CONNECTOR2/3V3_4 -> /INTERBOARD_CONNECTOR2/3V3_11
- J1 pad 6: 3V3 -> /INTERBOARD_CONNECTOR2/3V3_5
- J1 pad 7: /INTERBOARD_CONNECTOR2/SPARE_1 -> GND
- J1 pad 8: /INTERBOARD_CONNECTOR2/3V3_7 -> GND
- J1 pad 9: /INTERBOARD_CONNECTOR2/3V3_9 -> /INTERBOARD_CONNECTOR2/3V3_4
- J4 pad 1: +3V3 -> GND
- J4 pad 2: UART1_RTS -> +3V3
- J4 pad 3: UART1_RX -> /UART-CAN/MS_UART0_TX
- J4 pad 4: UART1_TX -> /UART-CAN/MS_UART0_RX
- J4 pad 5: UART1_CTS -> /UART-CAN/BSL
- J4 pad 6: GND -> /UART-CAN/RST_N
- J7 pad 2: GND -> +3V3
- J7 pad 5: /~{LST_RESET} -> unconnected-(J7-Pin_5-Pad5)
- J7 pad 6: +3V3 -> /~{LST_RESET}
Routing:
- net UART1_CTS: track 38.1 -> 3.44 mm
- net /UART-CAN/RST_N: track 0.00 -> 32.3 mm, vias 0 -> 1
- net +5V: track 122.3 -> 154.4 mm, vias 0 -> 2
- net /UART-CAN/BSL: track 0.00 -> 32.1 mm
- net CAN_L: track 0.00 -> 30.3 mm
- net CAN_H: track 0.00 -> 29.5 mm
- net /UART-CAN/SWCLK: track 0.00 -> 27.3 mm
- net /UART-CAN/SWDIO: track 0.00 -> 24.0 mm
- net /UART-CAN/MS_UART0_TX: track 0.00 -> 19.4 mm
- net /UART-CAN/MS_UART0_RX: track 0.00 -> 16.1 mm
- net /UART-CAN/CAN_RX: track 0.00 -> 13.8 mm
- net GND: track 229.9 -> 242.1 mm, vias 183 -> 194
- net /UART-CAN/CAN_TX: track 0.00 -> 11.0 mm
- net /UART-CAN/MS_UART1_TX: track 0.00 -> 10.3 mm
- net /UART-CAN/MS_UART1_RX: track 0.00 -> 7.92 mm
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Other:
- board text removed: "UART1"
